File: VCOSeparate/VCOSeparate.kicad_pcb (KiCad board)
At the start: 2 copper layers, 100 x 100 mm, 74 parts, among them IC1 V3340M, IC2 AS321KTR-E1, IC3 AS321KTR-E1, IC4 4013, J2 D_Power, J3 Output, J4 A_Power, J5 Input, Q18 Q_NPN_ECB

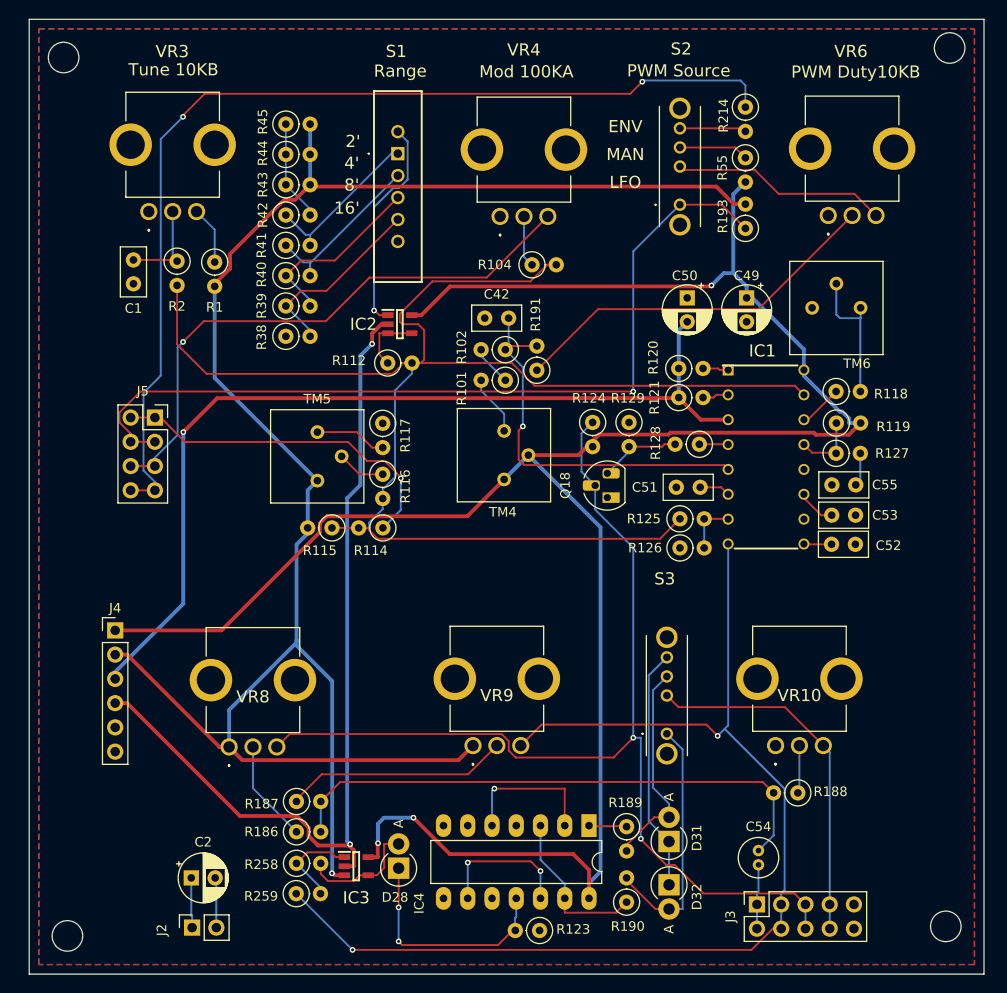
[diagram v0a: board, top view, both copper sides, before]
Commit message: MC2
VCO,VCF+VCA,Powerを登録
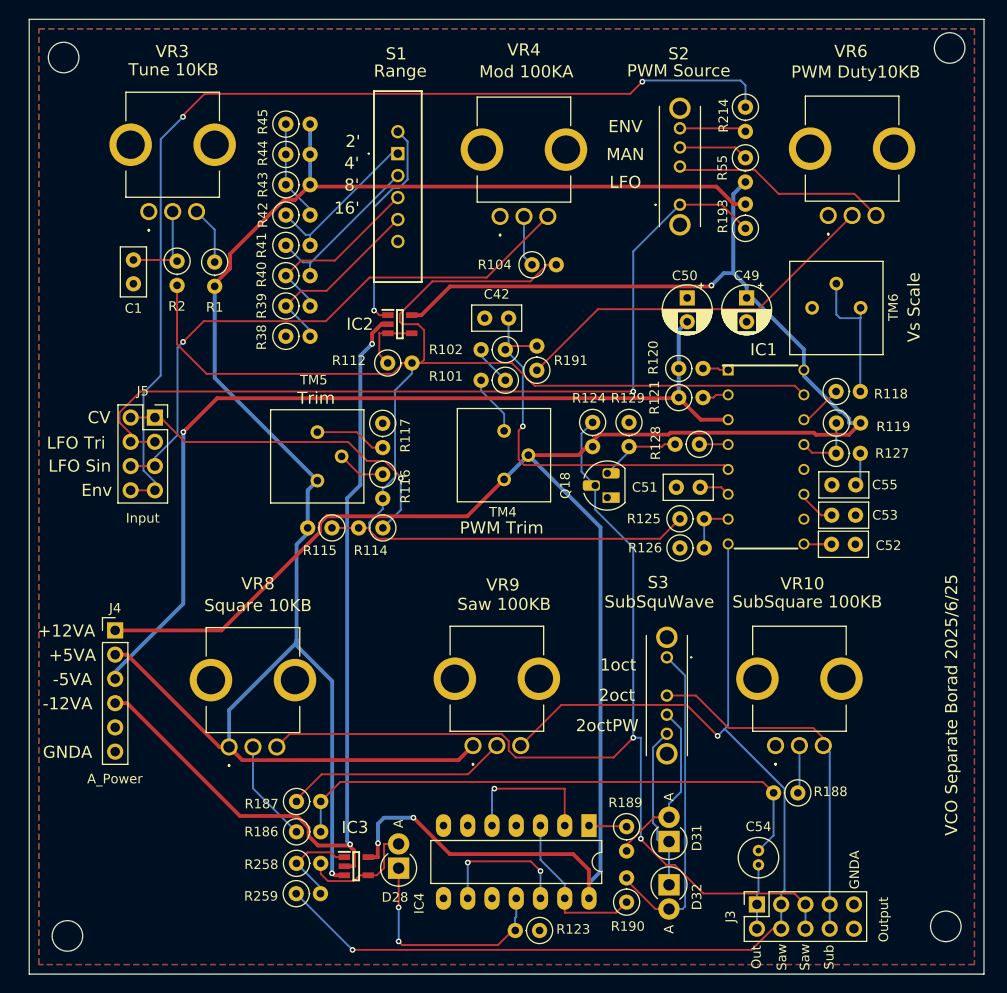
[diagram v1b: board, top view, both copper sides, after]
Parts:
- removed C2: 10uF/16V, Capacitor_THT:CP_Radial_D5.0mm_P2.50mm
- removed J2: D_Power, Connector_PinSocket_2.54mm:PinSocket_1x02_P2.54mm_Vertical
- turned S3 to -90 degrees
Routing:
- net Net-(D32-A): track 26.4 -> 34.6 mm
- net Net-(D31-K): track 25.5 -> 19.4 mm
- net GND: track 5.26 -> 0.00 mm
- net +5VD: track 5.24 -> 0.00 mm
- net Net-(D31-A): track 22.3 -> 18.2 mm
- net Vso: track 120.4 -> 122.1 mm
- net Net-(C52-Pad2): track 2.90 -> 4.33 mm
- net Net-(D28-K): track 24.0 -> 25.0 mm
- net Net-(C51-Pad2): track 3.23 -> 3.75 mm
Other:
- board text added: "+12VA"
- board text added: "+5VA"
- board text added: "-12VA"
- board text added: "-5VA"
- board text added: "1oct"
- board text added: "2oct"
- board text added: "2octPW"
- board text added: "A_Power"
- board text added: "CV"
- board text added: "Env"
- board text added: "GNDA"
- board text added: "Input"
- board text added: "LFO Sin"
- board text added: "LFO Tri"
- board text added: "Out"
- board text added: "Output"
- board text added: "PWM Trim"
- board text added: "Saw"
- board text added: "Saw 100KB"
- board text added: "Square 10KB"
- board text added: "Sub"
- board text added: "SubSquWave"
- board text added: "SubSquare 100KB"
- board text added: "Trim"
- board text added: "VCO Separate Borad 2025/6/25"
- board text added: "Vs Scale"

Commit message: MC2
ここまででFIXした内容
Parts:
- added C48: 0.01uF, Capacitor_THT:C_Disc_D5.0mm_W2.5mm_P2.50mm, F.Cu at (147.2, 83.4)
- added R113: 560, Resistor_THT:R_Axial_DIN0207_L6.3mm_D2.5mm_P2.54mm_Vertical, F.Cu at (155.1, 83.3)
- C54: footprint Capacitor_THT:C_Radial_D4.0mm_H7.0mm_P1.50mm -> Capacitor_THT:C_Radial_D6.3mm_H7.0mm_P2.50mm
- IC1: footprint SamacSys_Parts:DIP794W56P260L1905H432Q16N -> SamacSys_parts:DIP794W56P260L1905H432Q16N
- IC2, IC3: footprint SamacSys_Parts:SOT95P282X145-5N -> SamacSys_parts:SOT95P282X145-5N
- S1: footprint SamacSys_Parts:ASLB1470 -> SamacSys_parts:ASLB1470
- S2, S3: footprint SamacSys_Parts:OS103011MS8QP1 -> SamacSys_parts:OS103011MS8QP1
- VR10, VR3, VR4, VR6, VR8, VR9: footprint SamacSys_Parts:RK09D117000B -> SamacSys_parts:RK09D117000B
- moved C54 1.00 mm to (216.4, 137.1)
- moved Q18 0.67 mm to (201.2, 101.3)
- moved IC2 0.13 mm to (178.9, 82.9)
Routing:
- net Net-(C48-Pad2): track 0.00 -> 2.85 mm
- net Net-(C54-Pad1): track 58.6 -> 57.6 mm
- net Net-(C51-Pad2): track 3.75 -> 4.72 mm
- net Net-(C52-Pad2): track 4.33 -> 3.66 mm
- net Net-(C53-Pad2): track 4.04 -> 4.59 mm
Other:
- board text added: "VCO Separate Borad Rev.2 2025/8/16"
- board text removed: "VCO Separate Borad 2025/6/25"

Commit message: MC2
デバッグ一通り完了して動作出来た
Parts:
- added C2: 0.01uF, Capacitor_THT:C_Disc_D5.0mm_W2.5mm_P2.50mm, F.Cu at (226.7, 92.4)
- added J1: SyncIn, Connector_PinSocket_2.54mm:PinSocket_2x03_P2.54mm_Vertical, F.Cu at (230.1, 135.4)
- added J2: Output, Connector_PinSocket_2.54mm:PinSocket_2x06_P2.54mm_Vertical, F.Cu at (207.4, 142.6)
- added R3: 390K, Resistor_THT:R_Axial_DIN0207_L6.3mm_D2.5mm_P2.54mm_Vertical, F.Cu at (196.5, 131.2)
- added R4: 1M, Resistor_THT:R_Axial_DIN0207_L6.3mm_D2.5mm_P2.54mm_Vertical, F.Cu at (226.8, 100.3)
- added S4: SS14D0839VG5PA, SamacSys_parts:SS14D0839VG5PA, F.Cu at (178.8, 62.6)
- added VR1: Tri 100KB, SamacSys_parts:RK09D117000B, F.Cu at (193.9, 126.3)
- J3: value Output -> LFM Wave; footprint Connector_PinSocket_2.54mm:PinSocket_2x05_P2.54mm_Vertical -> Connector_PinSocket_2.54mm:PinSocket_2x03_P2.54mm_Vertical
- R1: value 100K -> 10K
- R186: value 680K -> 470K
- R187: value 390K -> 470K
- S1: value ASLB1470 -> LFM In; footprint SamacSys_parts:ASLB1470 -> SamacSys_parts:SS14D0839VG5PA
- moved J3 60.4 mm to (228.7, 84.6), turned to 180 degrees
- moved S1 59.9 mm to (232.4, 91.3)
- moved R112 17.9 mm to (171.4, 103.8), turned to 180 degrees
- moved IC2 17.9 mm to (171.9, 99.3)
- moved C42 16.9 mm to (174.6, 93.1), turned to 90 degrees
- moved R191 12.6 mm to (180.6, 87.2), turned to 180 degrees
- moved R102 12.4 mm to (178.5, 90.6), turned to -90 degrees
- moved R114 10.9 mm to (166.1, 103.6)
- moved R115 10.9 mm to (160.8, 103.6)
- moved R116 10.9 mm to (166.1, 98.0)
- moved R117 10.9 mm to (166.1, 92.7)
- moved TM5 10.9 mm to (159.3, 98.7)
- moved VR9 9.85 mm to (176.7, 126.4)
- moved C49 8.51 mm to (206.6, 79.9)
- moved C53 8.51 mm to (218.0, 102.6)
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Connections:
- C51 pad 1: GNDA -> HardSyncIn
- C52 pad 1: GNDA -> SoftSyncIn
- IC1 pad 10: unconnected-(IC1-Pad10) -> Vtri
- J3 pad 1: VCOWave -> Vso
- J3 pad 2: VCOWave -> Net-(J3-Pin_2)
- J3 pad 3: Vso -> VP
- J3 pad 4: Vso -> Net-(J3-Pin_4)
- J3 pad 5: VPseparate -> Vtri
- J3 pad 6: VPseparate -> Net-(J3-Pin_6)
- R38 pad 2: Net-(S1-NO_4) -> Net-(R38-Pad2)
- R39 pad 1: Net-(S1-NO_4) -> Net-(R38-Pad2)
- R39 pad 2: Net-(S1-NO_3) -> Net-(R39-Pad2)
- R40 pad 1: Net-(S1-NO_3) -> Net-(R39-Pad2)
- R40 pad 2: Net-(S1-NO_2) -> Net-(R40-Pad2)
- R41 pad 1: Net-(S1-NO_2) -> Net-(R40-Pad2)
- R41 pad 2: Net-(S1-NO_1) -> Net-(R41-Pad2)
- R42 pad 1: Net-(S1-NO_1) -> Net-(R41-Pad2)
- S1 pad 1: Net-(S1-NO_1) -> Net-(J3-Pin_2)
- S1 pad 2: Net-(S1-NO_2) -> Net-(J3-Pin_4)
- S1 pad 3: Net-(S1-NO_3) -> LFM_In
- S1 pad 4: Net-(S1-NO_4) -> Net-(J3-Pin_6)
- S1 pad 5: Net-(IC2-INPUT_+) -> GNDA
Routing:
- net Vtri: track 0.00 -> 96.6 mm, vias 0 -> 1
- net HardSyncIn: track 0.00 -> 64.5 mm, vias 0 -> 3
- net Vfci: track 160.5 -> 115.6 mm, vias 0 -> 1
- net SoftSyncIn: track 0.00 -> 41.3 mm
- net +12VA: track 239.0 -> 203.0 mm, vias 3 -> 1
- net VP: track 3.03 -> 32.5 mm
- net Vso: track 122.1 -> 148.1 mm, vias 2 -> 3
- net Net-(R40-Pad2): track 0.00 -> 21.4 mm
- net Net-(J3-Pin_6): track 0.00 -> 21.3 mm
- net Net-(D31-A): track 18.2 -> 38.9 mm, vias 0 -> 1
- net Net-(R41-Pad2): track 0.00 -> 20.2 mm
- net Net-(S1-NO_4): track 19.7 -> 0.00 mm
- net Net-(R38-Pad2): track 0.00 -> 19.7 mm
- net Net-(S1-NO_3): track 19.3 -> 0.00 mm
- net Net-(R39-Pad2): track 0.00 -> 19.2 mm
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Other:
- board text added: "Hard In"
- board text added: "LFM In"
- board text added: "None"
- board text added: "Soft In"
- board text added: "Squ"
- board text added: "Tri"
- board text added: "Triangle 100KB"
- board text added: "Trng"
- board text added: "VCO Separate Borad Rev.2 2025/8/31"
- board text removed: "VCO Separate Borad Rev.2 2025/8/16"
